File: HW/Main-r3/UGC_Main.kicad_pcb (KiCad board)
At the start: 4 copper layers, 125.7 x 76.4 mm, 138 parts, among them J1 SM02B-SURS-TF_LF__SN_, J13 503480-0640, J2 LT, J3 RT, J4 Conn_01x06_Pin, J5 UJ31-CH-G1-SMT-TR, J8 Conn_01x02, J9 Conn_01x02, Q1 MMBT3904, Q2 MMBT3904, Q3 BSS138DW, Q4 BSS138DW, Q5 Q_NMOS_GSD, SW1 SW_Push, SW10 SW_Push, SW11 SW_Push, SW12 SW_Push, SW13 SW_Push, SW14 TS09-63-25-R-260-SMT, SW15 1TS026A-1000-0550, SW16 1TS026A-1000-0550, SW17 TS09-63-25-R-260-SMT, SW18 TS09-63-25-R-260-SMT, SW19 TS09-63-25-R-260-SMT, SW2 SW_Push, SW20 TS09-63-25-R-260-SMT, SW3 SW_Push, SW4 SW_Push, SW6 GL18_SW, SW7 SW_Push, SW8 SW_Push, SW9 TS09-63-25-R-260-SMT, U1 ESP32-PICO-MINI-02, U10 ST_LSM6, U11 BQ25180, U12 CH340K, U13 PI3USB4000A, U2 GH39F (Hall SOT23), U3 GH39F (Hall SOT23), U4 TPS630001RCR, U5 ST_LSM6, U6 MCP3002, U7 MCP3002, U8 RP2040, U9 GD25Q80EEIGR, Y1 Crystal_GND3

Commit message: Update revision
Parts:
- moved L6 2.00 mm to (218.5, 142.6)
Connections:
- U8 pad 11: R_BRAKE -> LRA_HI
- U8 pad 5: RUMBLE -> LRA_HI
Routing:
- net LRA_HI: track 1.73 -> 33.7 mm, vias 0 -> 2
- net D: track 152.8 -> 159.5 mm
- net A: track 188.1 -> 191.1 mm, vias 5 -> 6
- net RUMBLE: track 1.89 -> 0.00 mm
- net PLAYER_RGB: track 41.8 -> 42.7 mm
- net ABXY_RGB: track 33.3 -> 34.2 mm
- net C: track 139.5 -> 138.7 mm, vias 6 -> 5
- net ESP_IO0: track 27.6 -> 28.4 mm
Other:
- board text removed: "MOTOR"

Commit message: Add cad files
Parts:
- removed SW20: TS09-63-25-R-260-SMT, hhl:TS09
- added D11: BAS16VY,115, Package_TO_SOT_SMD:SOT-363_SC-70-6, F.Cu at (188.0, 130.5)
- added D12: BAS16VY,115, Package_TO_SOT_SMD:SOT-363_SC-70-6, F.Cu at (212.0, 134.9)
- added D13: BAS16VY,115, Package_TO_SOT_SMD:SOT-363_SC-70-6, F.Cu at (212.0, 137.7)
- added D8: BAS16VY,115, Package_TO_SOT_SMD:SOT-363_SC-70-6, F.Cu at (185.1, 131.9)
- added SW5: SW_TS-1187A, hhl:TS-1187A-C-E-B, F.Cu at (218.5, 136.5)
- SW14, SW17, SW18, SW19, SW9: value TS09-63-25-R-260-SMT -> SW_TS-1187A; footprint hhl:TS09 -> hhl:TS-1187A-C-E-B
- moved SW9 17.5 mm to (222.9, 118.5), turned to 90 degrees
- moved SW18 11.8 mm to (222.9, 127.4)
- moved SW17 7.70 mm to (214.0, 118.5), turned to -90 degrees
- moved D5 3.57 mm to (239.6, 106.1)
- moved R33 3.34 mm to (220.6, 129.5)
- moved D4 3.32 mm to (238.8, 109.0)
- moved R5 2.59 mm to (230.6, 102.1)
- moved J1 2.31 mm to (219.4, 123.9), turned to 90 degrees
- moved SW16 2.16 mm to (207.8, 134.4), turned to 90 degrees
- moved U12 1.95 mm to (203.9, 123.2)
- moved SW15 1.68 mm to (226.6, 134.9)
- moved SW19 1.33 mm to (214.0, 127.4)
- moved J9 1.28 mm to (174.0, 136.3)
- moved C5 1.16 mm to (227.9, 101.6)
- moved C18 1.06 mm to (200.7, 126.2)
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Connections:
- D4 pad 1: Z -> Net-(D4A-A)
- D4 pad 2: X -> Net-(D4B-A)
- D4 pad 3: Y -> Net-(D4C-A)
- D4 pad 4: D -> C
- D4 pad 5: E -> B
- D4 pad 6: F -> A
- D5 pad 1: W -> Net-(D5A-A)
- D5 pad 2: unconnected-(D5B-A-Pad2) -> Net-(D5B-A)
- D5 pad 3: unconnected-(D5C-A-Pad3) -> Net-(D5C-A)
- D5 pad 4: unconnected-(D5C-K-Pad4) -> F
- D5 pad 5: unconnected-(D5B-K-Pad5) -> E
- D5 pad 6: C -> D
- J2 pad 1: W -> Net-(D11C-A)
- J2 pad 2: D -> H
- J3 pad 1: W -> Net-(D5C-A)
- J3 pad 2: E -> G
- J8 pad 1: F -> Net-(D4A-A)
- J8 pad 2: Y -> G
- J9 pad 1: F -> Net-(D11B-A)
- J9 pad 2: W -> H
- R34 pad 1: Z -> Net-(D4A-A)
- R35 pad 2: E -> G
- SW1 pad 1: A -> G
- SW1 pad 2: Z -> Net-(D4B-A)
- SW10 pad 1: A -> H
- SW10 pad 2: X -> Net-(D8A-A)
- SW11 pad 1: B -> H
- SW11 pad 2: X -> Net-(D8B-A)
- SW12 pad 1: C -> H
- SW12 pad 2: X -> Net-(D8C-A)
- SW13 pad 1: D -> I
- SW13 pad 2: X -> Net-(D13B-A)
- SW2 pad 1: B -> I
- SW2 pad 2: Z -> Net-(D13C-A)
- SW3 pad 1: C -> G
- SW3 pad 2: Z -> Net-(D4C-A)
- SW4 pad 1: D -> G
- SW4 pad 2: Z -> Net-(D5A-A)
- SW6 pad S1: F -> H
- SW6 pad S2: F -> H
- SW6 pad S3: X -> Net-(D11B-A)
- SW6 pad S4: X -> Net-(D11B-A)
- SW7 pad 1: A -> H
- SW7 pad 2: W -> Net-(D11A-A)
- SW8 pad 1: B -> G
- SW8 pad 2: W -> Net-(D5B-A)
- U1 pad 4: unconnected-(U1-I36-Pad4) -> BAT_LVL
- U8 pad 13: B -> I
- U8 pad 14: A -> H
- U8 pad 15: F -> G
- U8 pad 16: E -> F
- U8 pad 17: D -> E
- U8 pad 18: C -> D
- U8 pad 27: unconnected-(U8-GPIO16-Pad27) -> C
- U8 pad 28: unconnected-(U8-GPIO17-Pad28) -> B
- U8 pad 29: N_LATCH_3.3 -> A
- U8 pad 30: N_DATA_3.3 -> N_LATCH_3.3
- U8 pad 31: N_CLOCK_3.3 -> N_DATA_3.3
- U8 pad 32: RGB_OUT -> N_CLOCK_3.3
- U8 pad 39: ZR_ANALOG -> RGB_OUT
- U8 pad 40: BAT_LVL -> ZR_ANALOG
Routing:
- net W: track 230.9 -> 0.00 mm, vias 10 -> 0
- net H: track 0.00 -> 168.9 mm, vias 0 -> 9
- net X: track 163.4 -> 0.00 mm, vias 8 -> 0
- net I: track 0.00 -> 144.5 mm, vias 0 -> 5
- net G: track 0.00 -> 133.1 mm, vias 0 -> 11
- net Y: track 93.7 -> 0.00 mm, vias 4 -> 0
- net F: track 183.8 -> 95.2 mm, vias 9 -> 4
- net Z: track 88.0 -> 0.00 mm, vias 8 -> 0
- net A: track 191.1 -> 106.9 mm, vias 6 -> 4
- net Net-(D11A-A): track 0.00 -> 72.3 mm, vias 0 -> 3
- net Net-(D5C-A): track 0.00 -> 66.4 mm, vias 0 -> 3
- net Net-(D4A-A): track 0.00 -> 64.2 mm, vias 0 -> 6
- net D: track 159.5 -> 97.6 mm, vias 7 -> 4
- net B: track 158.9 -> 103.0 mm, vias 8 -> 4
- net Net-(D11B-A): track 0.00 -> 50.4 mm, vias 0 -> 2
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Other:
- outline, holes or cut-outs redrawn
- board text added: "GCU r3 Designed by Mitch"
- board text removed: "GCU v2 Designed by Mitch"

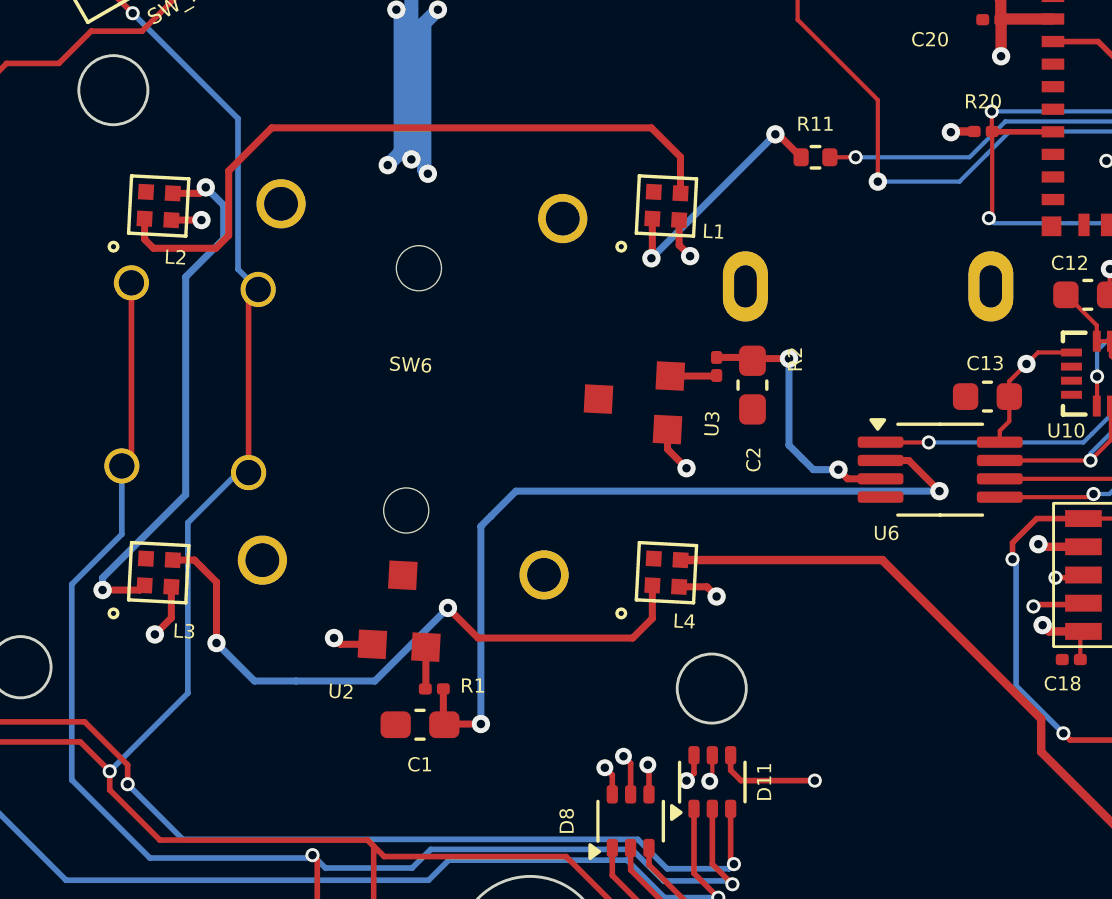
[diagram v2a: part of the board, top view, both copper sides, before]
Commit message: Main board update
Use new TMR stick on main board
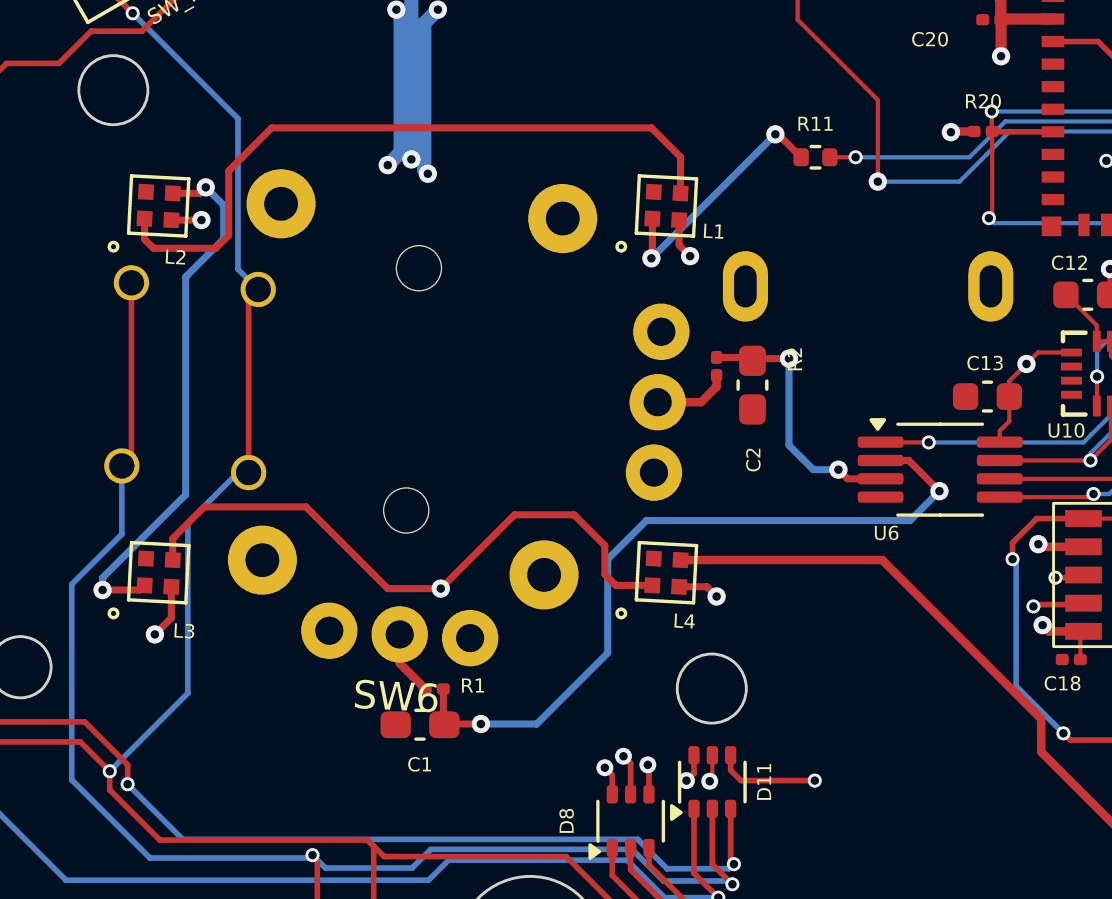
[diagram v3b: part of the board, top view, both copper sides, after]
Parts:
- removed U2, U3: GH39F (Hall SOT23), hhl:GH39F
- SW6: footprint hhl:GL18 -> hhl:GL1807SYAE
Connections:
- net Net-(D11B-A) renamed LS_BTN_IN
- R1 pad 1: Net-(U2-VOUT) -> Net-(SW6-X_OUT)
- R2 pad 1: Net-(U3-VOUT) -> Net-(SW6-Y_OUT)
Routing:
- net +3V3: track 128.0 -> 124.9 mm, vias 46 -> 44
- net Net-(SW6-Y_OUT): track 0.00 -> 2.74 mm
- net Net-(SW6-X_OUT): track 0.00 -> 2.34 mm
- net LX: track 28.9 -> 26.8 mm
- net Net-(U3-VOUT): track 1.65 -> 0.00 mm
- net Net-(U2-VOUT): track 1.49 -> 0.00 mm
- net Net-(L3-DOUT): track 23.0 -> 22.1 mm, vias 2 -> 1
